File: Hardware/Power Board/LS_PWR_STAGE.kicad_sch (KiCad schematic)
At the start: 49 parts, among them IC4 SN6507DGQR, IC5 UCC21755-Q1, IC6 TMP236A4DBZR, Q6 G3R40MT12J, Q7 G3R40MT12J, T2 782100_35JVC, U1 L78M05, U2 L78M15, U3 LM7905S

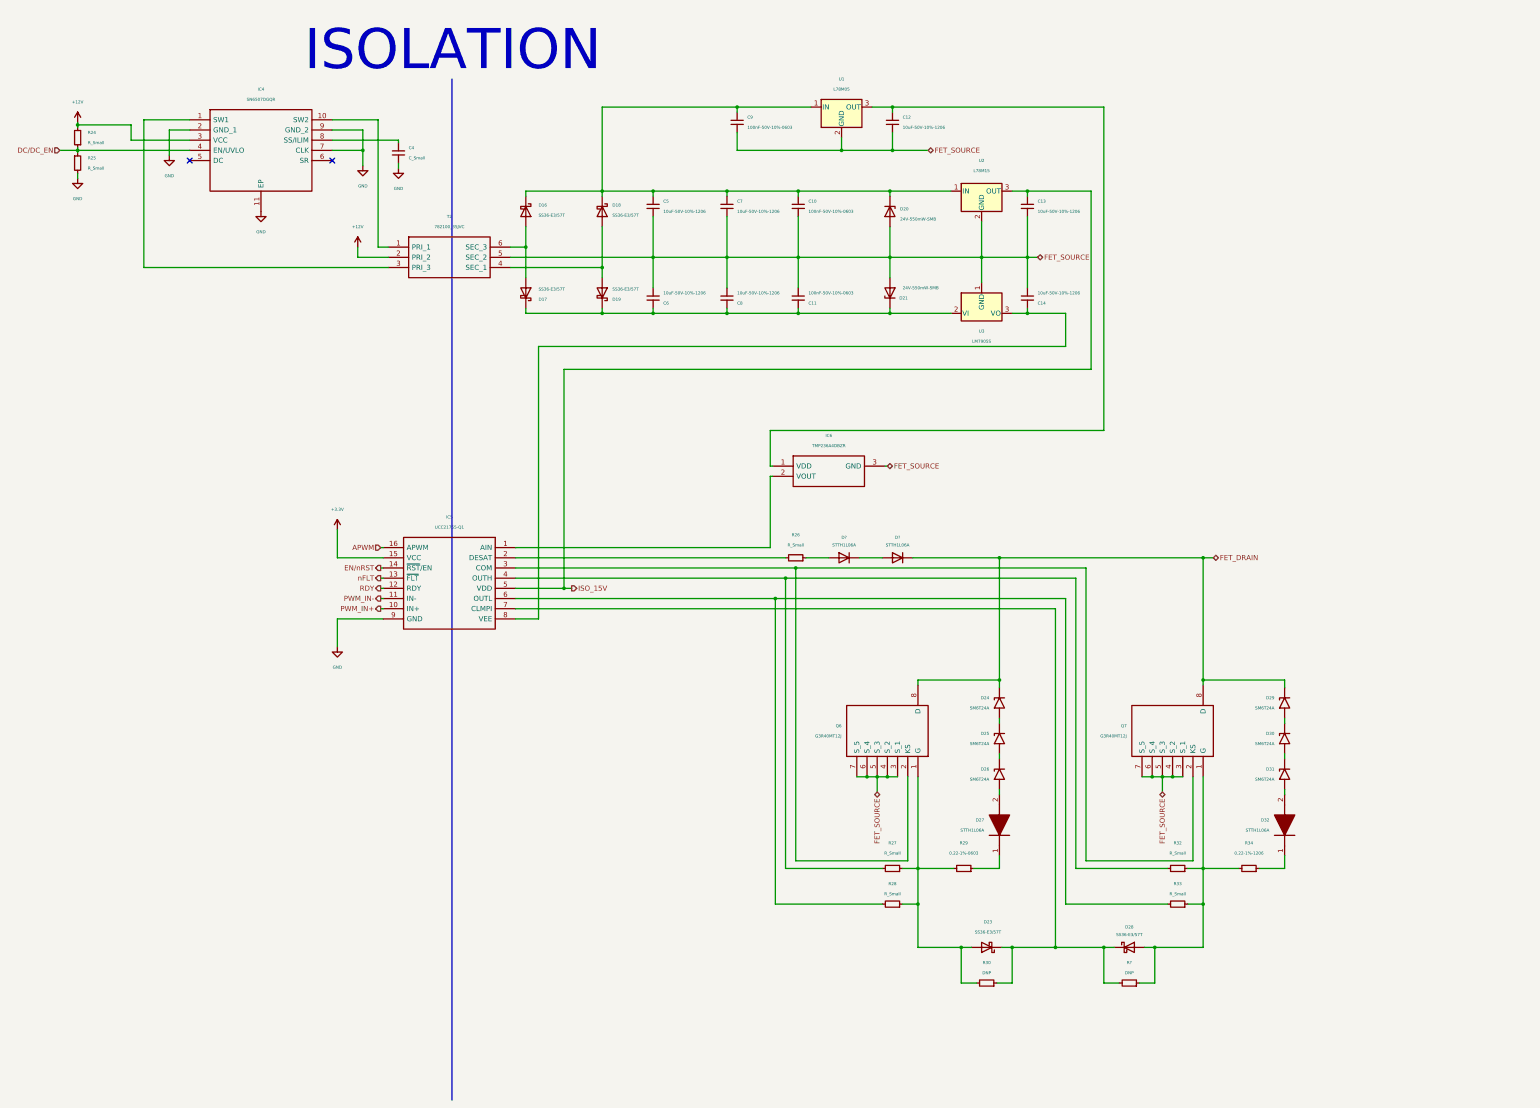
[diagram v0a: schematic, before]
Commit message: Updates to board, changed gate driver IC to one with external clamp
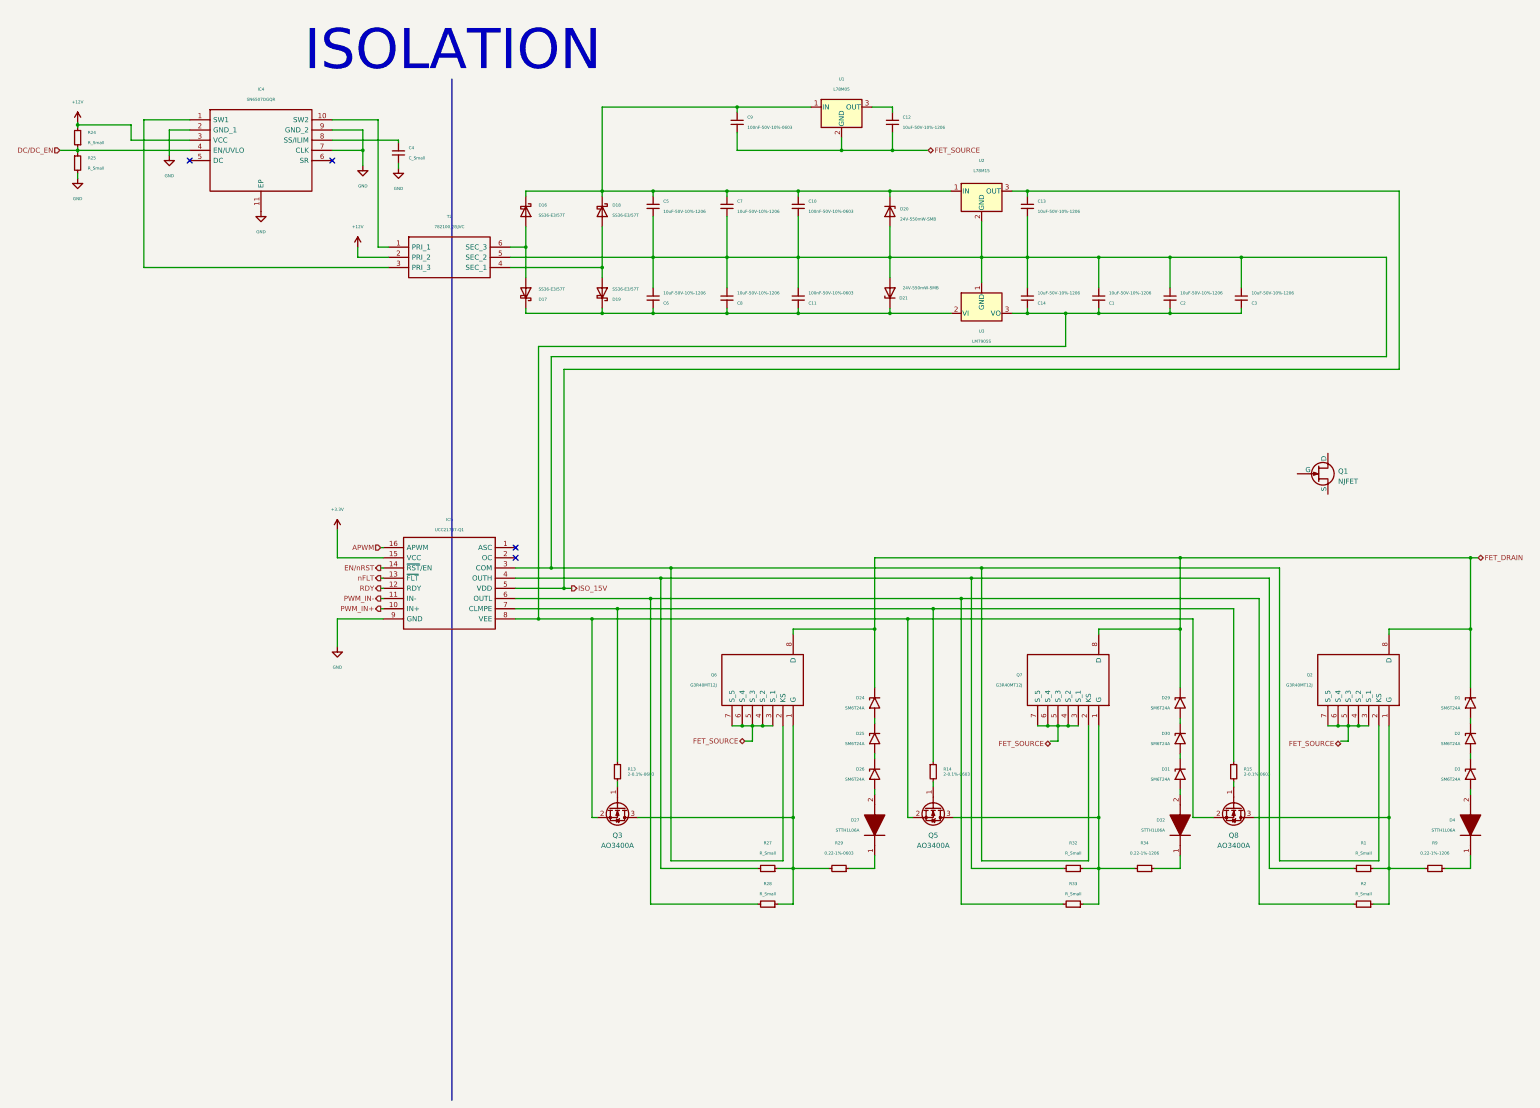
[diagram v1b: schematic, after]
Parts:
- removed D23, D28: SS36-E3/57T, Diode_SMD:D_SMC, symbol Device:D_Schottky
- removed D? (x2): STTH1L06A, DIOM5126X265N, symbol Device:D
- removed IC6: TMP236A4DBZR, SOT95P237X112-3N, symbol SamacSys_Parts:TMP236A4DBZR
- removed R26: R_Small, symbol Device:R_Small
- removed R30, R?: DNP, symbol Device:R_Small
- added C1, C2, C3: 10uF-50V-10%-1206, symbol Device:C_Small
- added D1, D2, D3: SM6T24A, Diode_SMD:D_SMB, symbol Diode:SM6T24A
- added D4: STTH1L06A, DIOM5126X265N, symbol SamacSys_Parts:STTH1L06A
- added Q1: NJFET, Library:HYG050N13NS1B6, symbol Simulation_SPICE:NJFET
- added Q2: G3R40MT12J, SamacSys_Parts:G3R40MT12J, symbol SamacSys_Parts:G3R40MT12J
- added Q3, Q5, Q8: AO3400A, Package_TO_SOT_SMD:SOT-23, symbol Transistor_FET:AO3400A
- added R1, R2: R_Small, symbol Device:R_Small
- added R13, R14, R15: 2-0.1%-0603, symbol Device:R_Small
- added R9: 0.22-1%-1206, symbol Device:R_Small
- IC5: value UCC21755-Q1 -> UCC21737-Q1
- Q7: footprint G3R40MT12J -> SamacSys_Parts:G3R40MT12J
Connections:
- net FET_DRAIN: now also D1.1 (A1), Q2.8 (D)
- net FET_SOURCE: no longer C10.1, C11.1, C13.1, C14.1, C5.1, C6.1, C7.1, C8.1, D20.2 (A), D21.2 (A), Q7.3 (S_1), Q7.4 (S_2), Q7.5 (S_3), Q7.6 (S_4), Q7.7 (S_5), T2.5 (SEC_2), U2.2 (GND), U3.1 (GND)
- net at IC5.7 (CLMPE): now also R13.1, R14.1, R15.1
- net at Q6.1 (G), R27.1, R28.1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: now also Q3.3 (D)
- net at C14.2, IC5.8 (VEE), U3.3 (VO): now also C1.2, C2.2, C3.2, Q3.2 (S), Q5.2 (S), Q8.2 (S)
- net at Q7.1 (G), R32.1, R33.1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: now also Q5.3 (D)
- net at IC5.3 (COM), Q6.2 (KS), Q7.2 (KS): now also C10.1, C11.1, C13.1, C14.1, C5.1, C6.1, C7.1, C8.1, D20.2 (A), D21.2 (A), T2.5 (SEC_2), U2.2 (GND), U3.1 (GND), C1.1, C2.1, C3.1, Q2.2 (KS)
- net at IC5.4 (OUTH), R27.2, R32.2: now also R1.2
- net at IC5.6 (OUTL), R28.2, R33.2: now also R2.2
- new net: D1.2 (A2), D2.1 (A1)
- new net: D2.2 (A2), D3.1 (A1)
- new net: D4.1, R9.1
- new net: Q2.1 (G), Q8.3 (D), R1.1, R2.1, R9.2
- new net: D3.2 (A2), D4.2
- new net: Q2.3 (S_1), Q2.4 (S_2), Q2.5 (S_3), Q2.6 (S_4), Q2.7 (S_5)
- new net: Q5.1 (G), R14.2
- new net: Q7.3 (S_1), Q7.4 (S_2), Q7.5 (S_3), Q7.6 (S_4), Q7.7 (S_5)
- new net: Q3.1 (G), R13.2
- new net: Q8.1 (G), R15.2
- no-connect marks 2 -> 4
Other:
- moved on the sheet: D24, D25, D26, D27, D29, D30, D31, D32, Q6, Q7, R27, R28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

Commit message: Ditched ASC
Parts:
- removed R24, R25: R_Small, symbol Device:R_Small
- removed U1: L78M05, Package_TO_SOT_SMD:TO-252-2, symbol Regulator_Linear:L7805
- added C32: 10uF-50V-10%-1206, symbol Device:C_Small
- added C33: 100nF-50V-10%-0603, symbol Device:C_Small
- added R3: 0-10%-0603, symbol Device:R_Small
- added R4: 50k-1%-0603, symbol Device:R_Small
- C1, C12, C2, C3: value 10uF-50V-10%-1206 -> 100nF-50V-10%-0603
- C4: value C_Small -> 500nF-50V-10%-0603
- C9: value 100nF-50V-10%-0603 -> 10uF-50V-10%-1206
- Q6: footprint G3R40MT12J -> SamacSys_Parts:G3R40MT12J
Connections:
- net FET_SOURCE: no longer C12.1, C9.1
- net GND: now also R3.2, R4.1; no longer IC4.7 (CLK)
- net ISO_15V: now also C12.2, C9.2
- net at C1.1, C10.1, C11.1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: now also C12.1, C9.1, C32.1, C33.1
- net at C10.2, C5.2, C7.2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: no longer C9.2
- net at C1.2, C14.2, C2.2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: now also C32.2, C33.2
- net at IC4.1 (SW1): now also T2.1 (PRI_1); no longer T2.3 (PRI_3)
- net at IC4.10 (SW2): now also T2.3 (PRI_3); no longer T2.1 (PRI_1)
- net at C4.2, IC4.8 (SS/ILIM): now also R4.2
- net +12V renamed +9V
- new net: IC4.7 (CLK), R3.1
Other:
- moved on the sheet: C4

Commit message: departure commit
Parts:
- added C34, C35: 1uF-25V-10%-0603, Capacitor_SMD:C_0603_1608Metric, symbol Device:C_Small
- added C36, C37, C38, C39, C40, C41: 10uF-100V-10%-2220, Capacitor_SMD:C_2220_5650Metric, symbol Device:C_Small
- C10, C11, C12, C2, C3: footprint (none) -> Capacitor_SMD:C_0603_1608Metric
- R13, R14: value 2-0.1%-0603 -> 2-1%-0603
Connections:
- net +3.3V: now also C35.1
- net +9V: now also C34.1
- net FET_DRAIN: now also C36.1, C37.1, C38.1, C39.1, C40.1, C41.1
- net FET_SOURCE: now also Q2.3 (S_1), Q2.4 (S_2), Q2.5 (S_3), Q2.6 (S_4), Q2.7 (S_5), Q7.3 (S_1), Q7.4 (S_2), Q7.5 (S_3), Q7.6 (S_4), Q7.7 (S_5), C36.2, C37.2, C38.2, C39.2, C40.2, C41.2
- net GND: now also C34.2, C35.2
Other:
- moved on the sheet: Q1

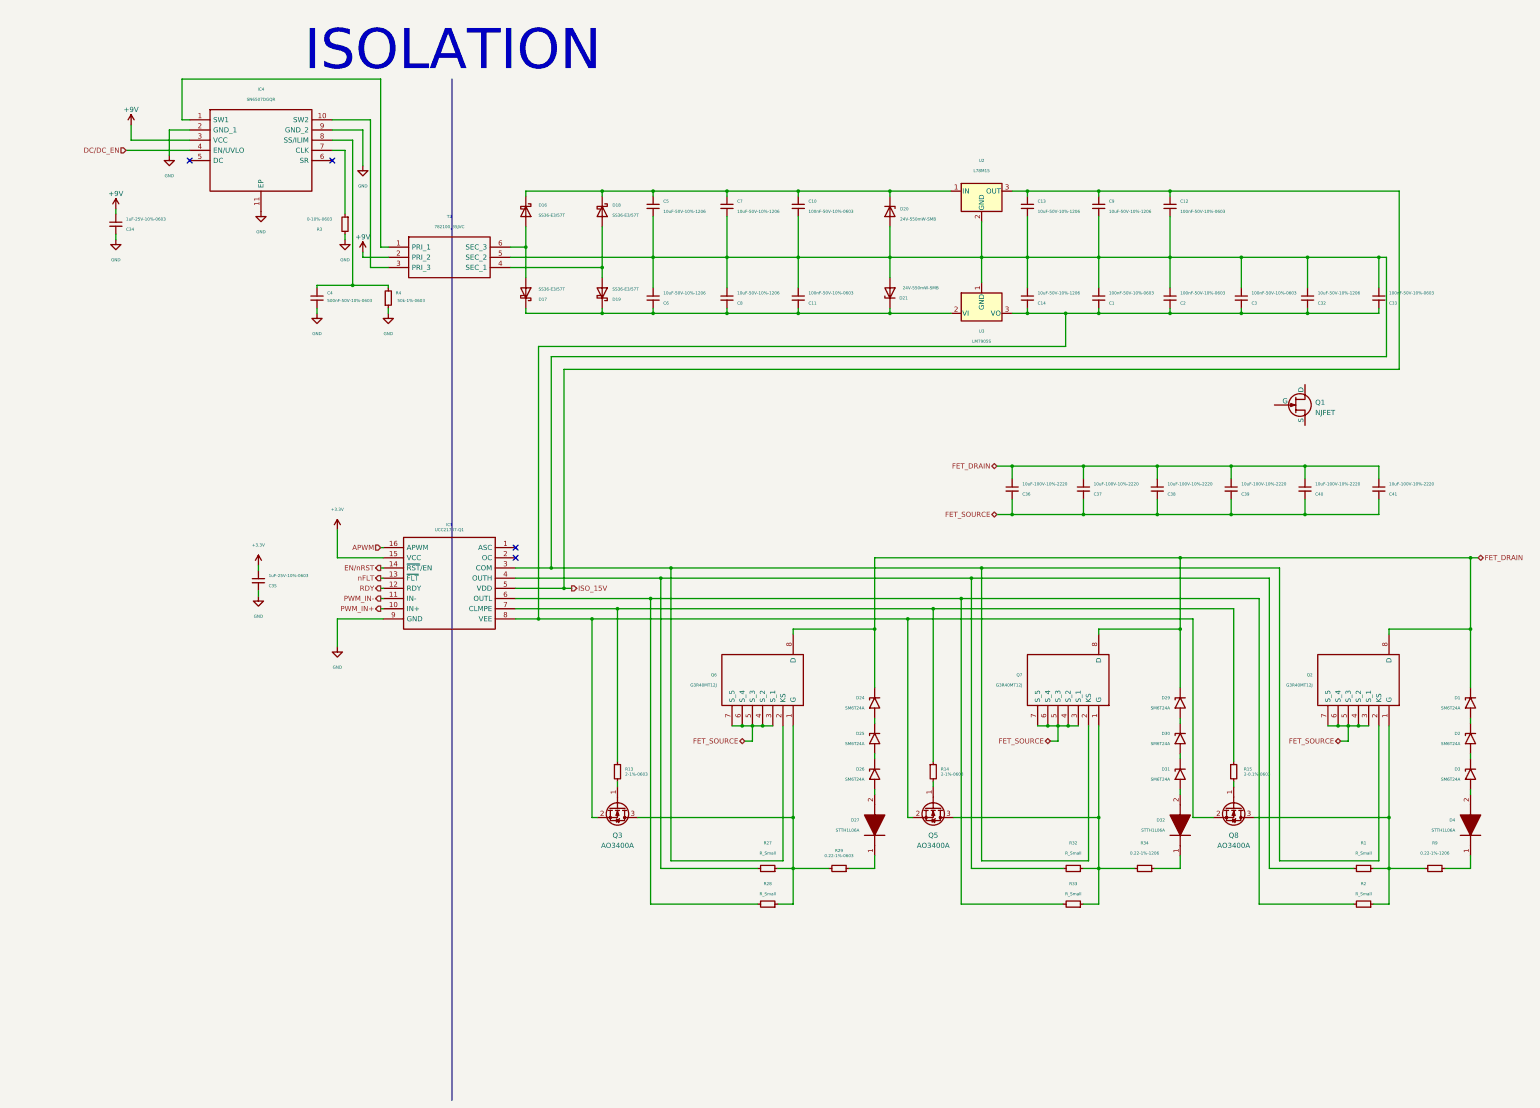
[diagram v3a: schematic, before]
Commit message: Board Layout Almost Done, about to remove Kelvin source due to concerns about uneven current sharing
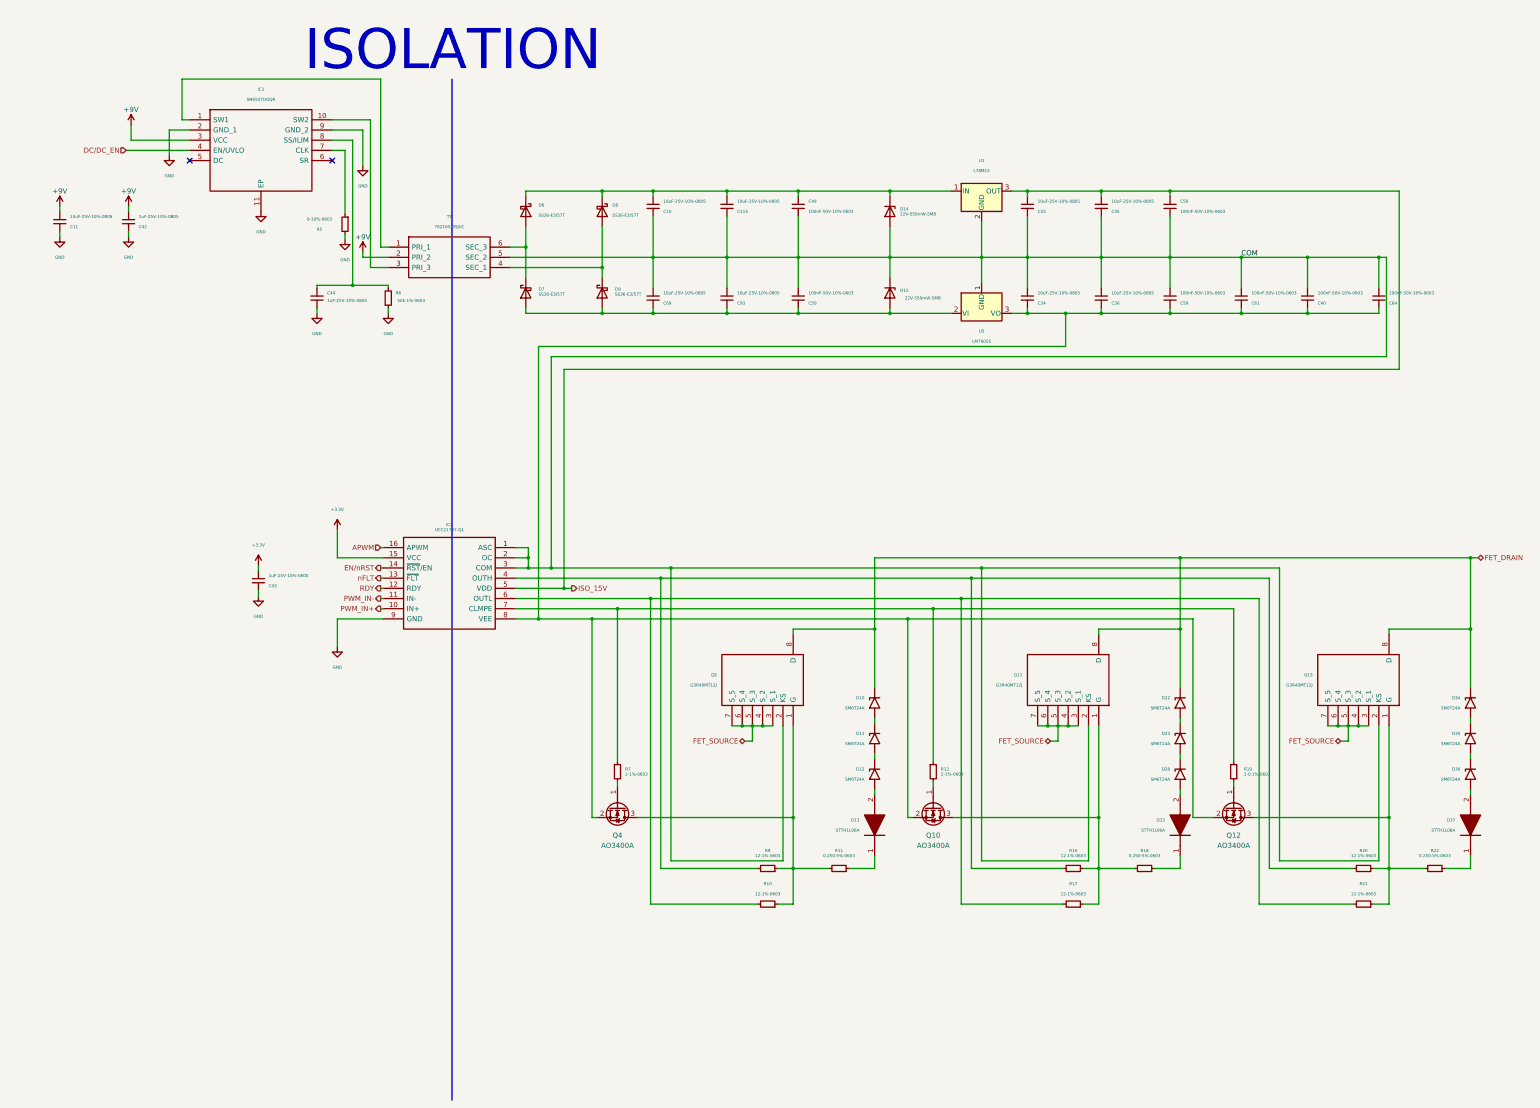
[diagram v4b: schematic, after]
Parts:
- removed C1: 100nF-50V-10%-0603, symbol Device:C_Small
- removed C13, C14, C32, C5, C6, C7, C8, C9: 10uF-50V-10%-1206, symbol Device:C_Small
- removed C37, C38, C39, C41: 10uF-100V-10%-2220, Capacitor_SMD:C_2220_5650Metric, symbol Device:C_Small
- removed Q1: NJFET, Library:HYG050N13NS1B6, symbol Simulation_SPICE:NJFET
- removed R34, R9: 0.22-1%-1206, symbol Device:R_Small
- added C10, C11, C114, C33, C34, C35, C69, C93: 10uF-25V-10%-0805, Capacitor_SMD:C_0805_2012Metric, symbol Device:C_Small
- added R18, R22: 0.250-5%-0603, Resistor_SMD:R_0603_1608Metric, symbol Device:R_Small
- C36: value 10uF-100V-10%-2220 -> 10uF-25V-10%-0805; footprint Capacitor_SMD:C_2220_5650Metric -> Capacitor_SMD:C_0805_2012Metric
- C40: value 10uF-100V-10%-2220 -> 100nF-50V-10%-0603; footprint Capacitor_SMD:C_2220_5650Metric -> Capacitor_SMD:C_0603_1608Metric
- C42: renamed from C34; value 1uF-25V-10%-0603 -> 1uF-25V-10%-0805; footprint Capacitor_SMD:C_0603_1608Metric -> Capacitor_SMD:C_0805_2012Metric
- C43: renamed from C35; value 1uF-25V-10%-0603 -> 1uF-25V-10%-0805; footprint Capacitor_SMD:C_0603_1608Metric -> Capacitor_SMD:C_0805_2012Metric
- C44: renamed from C4; value 500nF-50V-10%-0603 -> 1uF-25V-10%-0805; footprint (none) -> Capacitor_SMD:C_0805_2012Metric
- C64: renamed from C33; footprint (none) -> Capacitor_SMD:C_0603_1608Metric
- D13: renamed from D27; footprint DIOM5126X265N -> Diode_SMD:D_SMA
- D14: renamed from D20; value 24V-550mW-SMB -> 22V-550mW-SMB
- D15: renamed from D21; value 24V-550mW-SMB -> 22V-550mW-SMB
- D33: renamed from D32; footprint DIOM5126X265N -> Diode_SMD:D_SMA
- D37: renamed from D4; footprint DIOM5126X265N -> Diode_SMD:D_SMA
- R10: renamed from R28; value R_Small -> 12-1%-0603; footprint (none) -> Resistor_SMD:R_0603_1608Metric
- R11: renamed from R29; value 0.22-1%-0603 -> 0.250-5%-0603; footprint (none) -> Resistor_SMD:R_0603_1608Metric
- R12: renamed from R14; footprint (none) -> Resistor_SMD:R_0603_1608Metric
- R16: renamed from R32; value R_Small -> 12-1%-0603; footprint (none) -> Resistor_SMD:R_0603_1608Metric
- R17: renamed from R33; value R_Small -> 12-1%-0603; footprint (none) -> Resistor_SMD:R_0603_1608Metric
- R19: renamed from R15; footprint (none) -> Resistor_SMD:R_0603_1608Metric
- R20: renamed from R1; value R_Small -> 12-1%-0603; footprint (none) -> Resistor_SMD:R_0603_1608Metric
- R21: renamed from R2; value R_Small -> 12-1%-0603; footprint (none) -> Resistor_SMD:R_0603_1608Metric
- R5: renamed from R3; footprint (none) -> Resistor_SMD:R_0603_1608Metric
- R6: renamed from R4; footprint (none) -> Resistor_SMD:R_0603_1608Metric
- R7: renamed from R13; footprint (none) -> Resistor_SMD:R_0603_1608Metric
- R8: renamed from R27; value R_Small -> 12-1%-0603; footprint (none) -> Resistor_SMD:R_0603_1608Metric
- T1: renamed from T2; footprint 78210035JVC -> SamacSys_Parts:78210035JVC
- renumbered C10 to C49, C11 to C50, C12 to C58, C2 to C59, C3 to C61, D24 to D10, D25 to D11, D26 to D12, D29 to D22, D30 to D23, D31 to D28, D1 to D34, D2 to D35, D3 to D36, D16 to D6, D17 to D7, D18 to D8, D19 to D9, IC4 to IC1, IC5 to IC2, Q5 to Q10, Q7 to Q11, Q8 to Q12, Q2 to Q13, Q3 to Q4, Q6 to Q9, U2 to U1, U3 to U5
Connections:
- net +9V: now also C11.1
- net FET_DRAIN: no longer C36.1, C40.1
- net FET_SOURCE: no longer C36.2, C40.2
- net GND: now also C11.2
- net ISO_15V: now also C33.1, C35.1
- net COM: now reaches C49.1, C50.1, C58.1, C59.1, C61.1, C64.1, D14.2 (A), IC2.3 (COM), Q11.2 (KS), Q13.2 (KS), Q9.2 (KS), T1.5 (SEC_2), U1.2 (GND), U5.1 (GND)
- net COM: now also C36.1, C40.1, D15.1 (K), IC2.1 (ASC), IC2.2 (OC), C10.2, C114.2, C33.2, C34.1, C35.2, C69.1, C93.1; no longer D15.2 (A)
- net at D6.2 (A), T1.6 (SEC_3): now also D7.1 (K); no longer D7.2 (A)
- net at C59.2, C61.2, C64.2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: now also C36.2, C40.2, C34.2
- net at D8.2 (A), T1.4 (SEC_1): now also D9.1 (K); no longer D9.2 (A)
- net at D33.1: now also R18.1
- net at Q10.3 (D), Q11.1 (G), R16.1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: now also R18.2
- net at C49.2, D14.1 (K), D6.1 (K)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: now also C10.1, C114.1
- net at D37.1: now also R22.1
- net at Q12.3 (D), Q13.1 (G), R20.1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: now also R22.2
- new net: C50.2, C69.2, C93.2, D15.2 (A), D7.2 (A), D9.2 (A), U5.2 (VI)
- no-connect marks 4 -> 2
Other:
- moved on the sheet: C42, D15, D7, D9
